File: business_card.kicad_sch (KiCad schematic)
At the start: 10 parts, among them Q1 2N3904, U1 TLC555IP

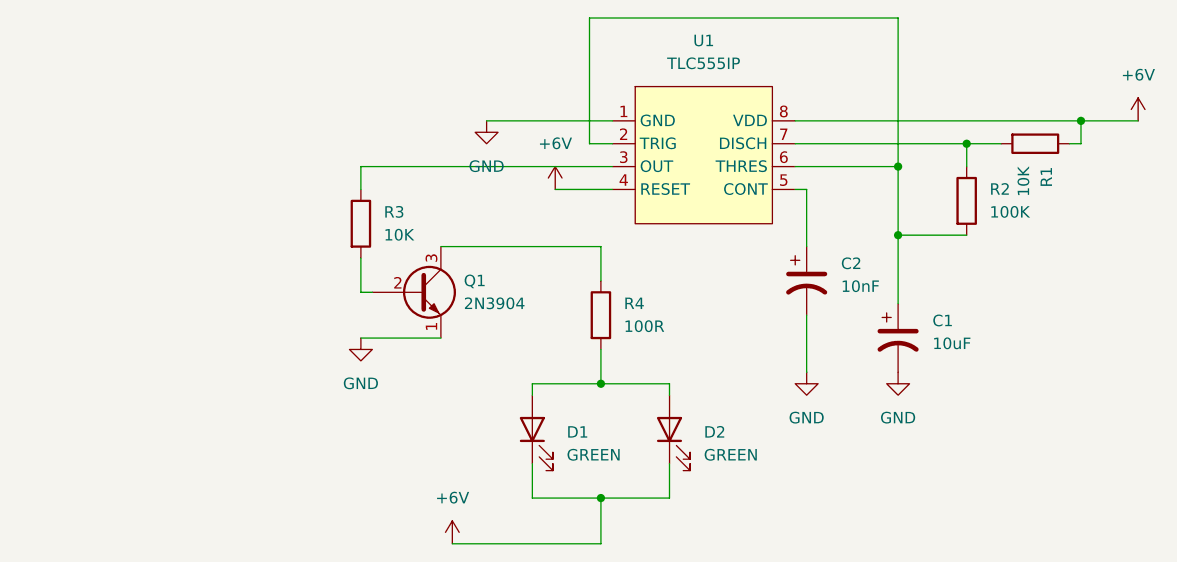
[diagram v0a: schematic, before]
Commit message: Add schematic and footprints
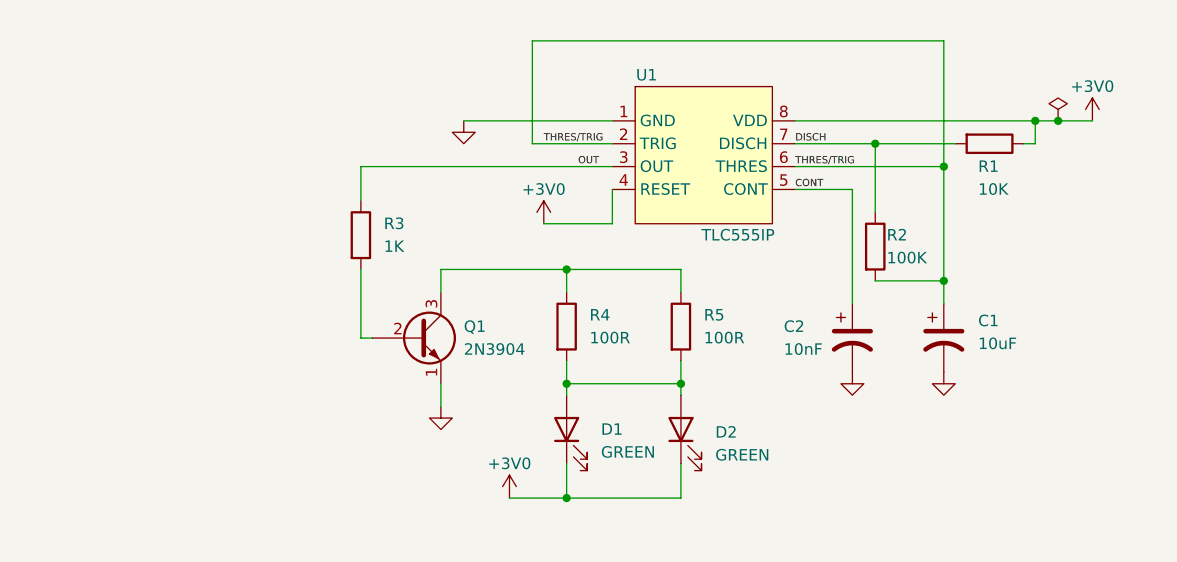
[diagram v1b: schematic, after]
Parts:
- added R5: 100R, Resistor_THT:R_Axial_DIN0207_L6.3mm_D2.5mm_P10.16mm_Horizontal, symbol Device:R
- C1: footprint (none) -> Capacitor_THT:CP_Radial_D4.0mm_P2.00mm
- C2: footprint (none) -> Capacitor_THT:CP_Radial_Tantal_D6.0mm_P5.00mm
- D1, D2: footprint (none) -> LED_THT:LED_D3.0mm
- R1, R2, R4: footprint (none) -> Resistor_THT:R_Axial_DIN0207_L6.3mm_D2.5mm_P10.16mm_Horizontal
- R3: value 10K -> 1K; footprint (none) -> Resistor_THT:R_Axial_DIN0207_L6.3mm_D2.5mm_P10.16mm_Horizontal
- U1: footprint (none) -> business_card:TLC555IP
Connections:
- net at Q1.3 (C), R4.1: now also R5.1
- net at D1.2 (A), D2.2 (A), R4.2: now also R5.2
- net CONT: now reaches C2.1, U1.5 (CONT)
- net THRES/TRIG: now reaches C1.1, R2.2, U1.2 (TRIG), U1.6 (THRES)
- net OUT: now reaches R3.1, U1.3 (OUT)
- net DISCH: now reaches R1.2, R2.1, U1.7 (DISCH)
- net +6V renamed +3V0
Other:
- moved on the sheet: C1, C2, D1, D2, Q1, R1, R2, R3, R4

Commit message: Add battery holder schematic, footprint and 3d model
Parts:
- added BT1: BAT-HLD-001-THM, business_card:BAT-HLD-001-THM, symbol Device:Battery_Cell
- added SW1: SW_SPST, symbol Switch:SW_SPST
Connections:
- net +3V0: now also SW1.1 (A)
- net GND: now also BT1.2 (-)
- new net: BT1.1 (+), SW1.2 (B)
